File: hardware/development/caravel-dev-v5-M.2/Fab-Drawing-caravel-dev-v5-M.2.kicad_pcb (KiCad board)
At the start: 2 copper layers, 76.2 x 73.8 mm, 70 parts, among them J1 USB_B_Micro, J10 Conn_01x28_Pin, J11 Conn_01x28_Pin, J12 Conn_01x04_Pin, J2 Conn_01x02_Pin, J3 Conn_01x02_Pin, J4 Conn_01x03_Pin, J5 Conn_01x02_Pin, J6 Conn_01x02_Pin, J7 Conn_01x06_Pin, J8 Conn_01x02_Pin, J9 Conn_01x02_Pin, SW1 SW_Push - SKQGADE010, T1 Logo, T2 Logo, U1 FT232H, U2 SN74LVC1G125DCKR, U3 SN74LVC1G125DCKR, U5 TAR5SxxU, U6 TAR5SxxU, U7 W25Q32FVSS, U8 M.2-CONNECTOR-E, X1 DSC6001_10MHZ, Y1 12MHz

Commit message: ~ update caravel REV 5B PCB
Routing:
- net /ACBUS1: track 126.3 -> 129.3 mm
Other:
- board text removed: "SW1"

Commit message: ~ update caravel REV 5B PCB
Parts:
- moved J1 0.06 mm to (131.9, 119.2)
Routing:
- net /ACBUS1: track 129.3 -> 128.8 mm
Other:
- board text added: "SW1"

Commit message: ~ enhance caravel REV 5B power tracks
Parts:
- moved J1 0.08 mm to (132.0, 119.2)
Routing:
- net +3V3: track 403.3 -> 385.0 mm
- net +1V8: track 245.2 -> 243.7 mm

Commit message: ~ update caravel REV 5B fab drawing
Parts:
- T1: footprint Caravel_Board:logo -> Caravel_Board:logo_large
- T2: footprint Caravel_Board:ef_logo -> Caravel_Board:ef_logo_large
- moved T1 2.92 mm to (136.0, 148.8)
- moved T2 2.81 mm to (136.0, 142.0)

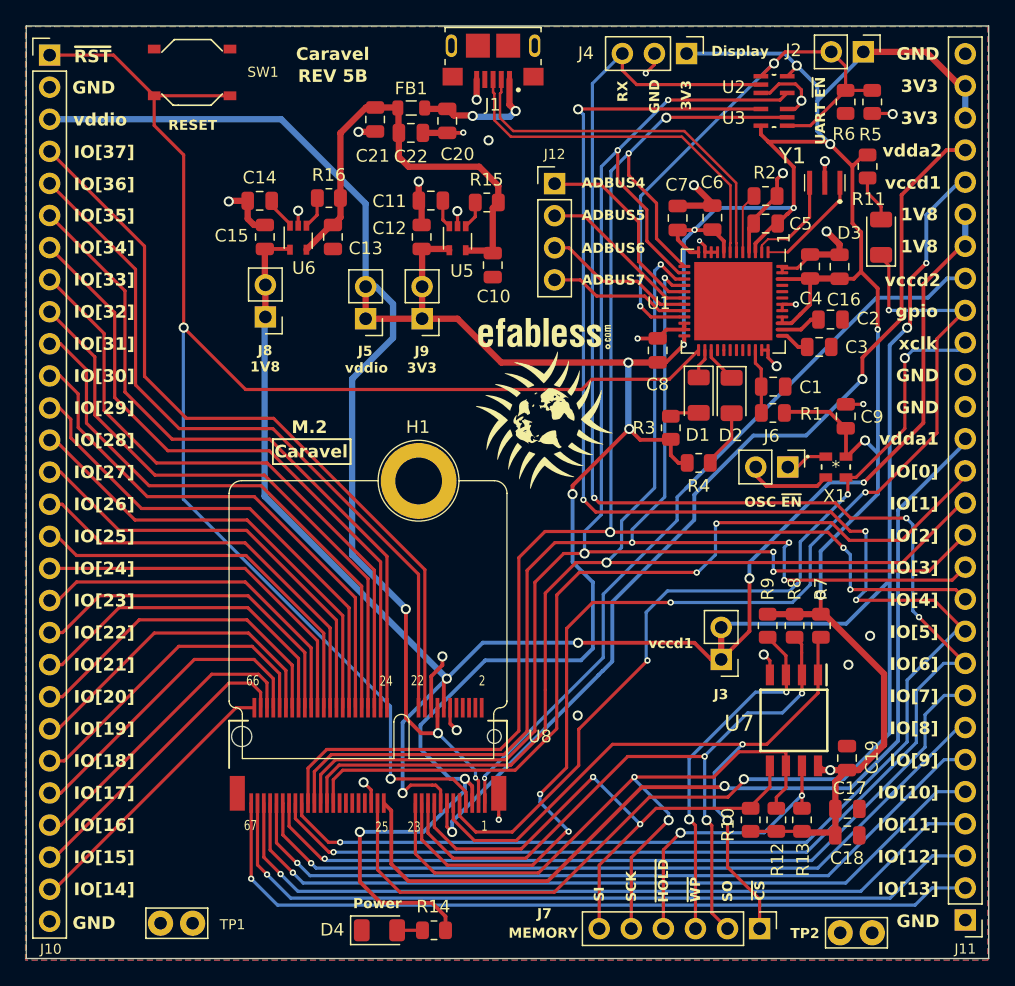
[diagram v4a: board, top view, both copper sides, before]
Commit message: ~ update caravel REV 5B logos
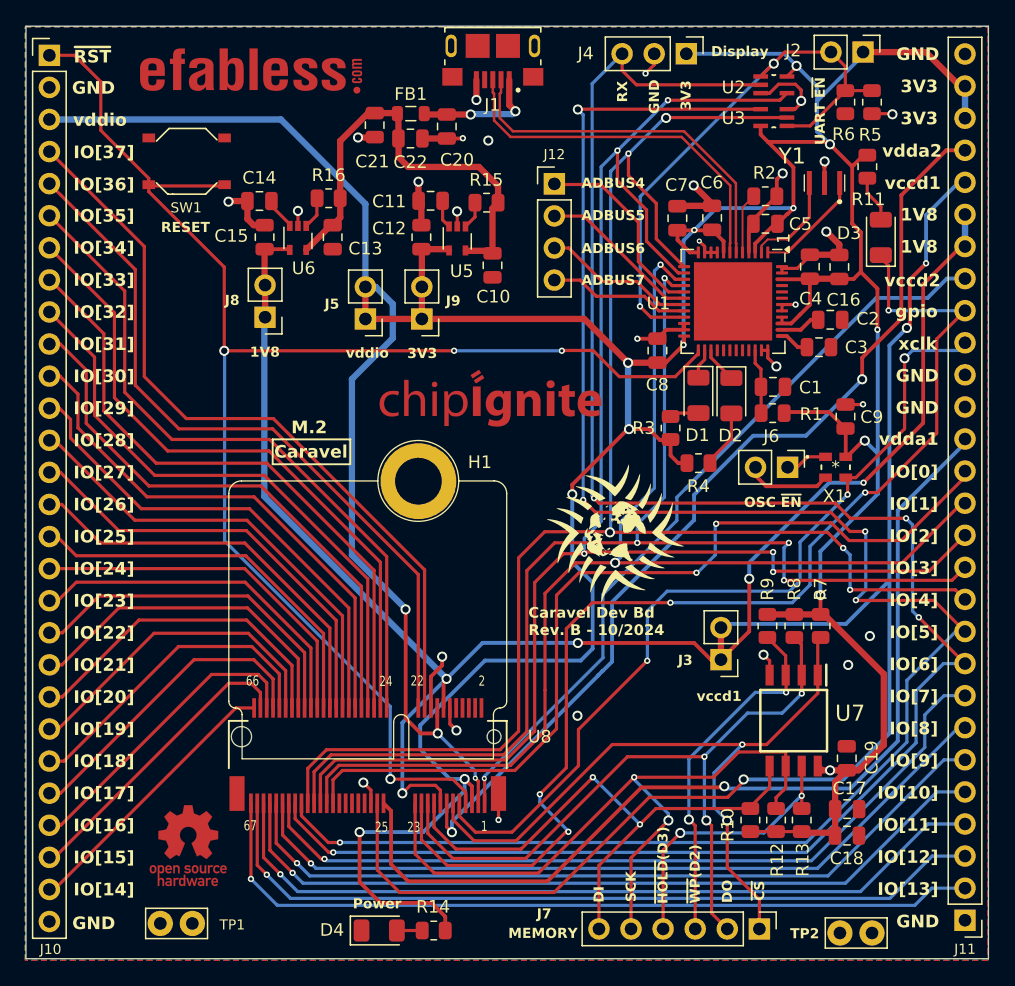
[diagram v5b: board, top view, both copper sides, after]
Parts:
- added T3: oshw logo CU, Caravel_Board:oshw-logo, F.Cu at (107.9, 182.6)
- added T4: ci logo CU, Caravel_Board:chipIgnite_logo, F.Cu at (139.2, 146.5)
- T1: value Logo -> ef world logo
- T2: value Logo -> ef logo CU; footprint Caravel_Board:ef_logo_large -> Caravel_Board:ef_logo-cu
- moved T2 33.9 mm to (110.1, 120.2)
- moved T1 10.6 mm to (141.6, 157.8)
- moved SW1 7.05 mm to (107.8, 128.4)
- moved C20 0.45 mm to (128.3, 125.6)
- moved C21 0.45 mm to (122.6, 125.5)
- moved C22 0.45 mm to (125.5, 126.6)
- moved FB1 0.45 mm to (125.5, 124.6)
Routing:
- net /ACBUS1: track 128.8 -> 122.2 mm, vias 2 -> 4
- net +5V: track 36.3 -> 35.5 mm
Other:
- board text added: "Caravel Dev Bd Rev. B - 10/2024"
- board text added: "DI"
- board text added: "DO"
- board text added: "~{HOLD}(D3)"
- board text added: "~{WP}(D2)"
- board text removed: "REV 5B"
- board text removed: "SI"
- board text removed: "SO"
- board text removed: "SW1"
- board text removed: "~{HOLD}"
- board text removed: "~{WP}"
